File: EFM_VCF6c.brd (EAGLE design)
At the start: 100 x 80.6 mm, 69 parts, among them IC1 LM13700N, Q1 2N3904, Q2 2N3904, Q3 2N3904, Q4 2N3904, Q5 2N3906, U1 POWER

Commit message: fix and mod for self res
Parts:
- Q3: value 2N3904 -> 2N3906; device transistor-npn:TO92 -> transistor-pnp:TO92
- R26: value 47k -> 100k
- moved Q4 31.3 mm to (57.8, 46.4), turned to 0 degrees
- moved Q2 25.3 mm to (27.9, 55.9), turned to 90 degrees
- moved Q3 5.75 mm to (52.1, 47.0), turned to 180 degrees
- moved C6 0.25 mm to (63.5, 61.2)
- moved C7 0.25 mm to (55.9, 61.2)
- moved C8 0.25 mm to (48.3, 61.2)
- moved C9 0.25 mm to (40.6, 61.2)
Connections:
- net -12V: now also Q3.1; no longer Q2.1
- net GND: now also Q4.3; no longer Q3.3
- net N$16: now also Q3.2; no longer Q2.2
- net N$20: now also Q2.1; no longer Q4.1
- net N$26: now also Q2.2; no longer Q4.2
- net N$3: now also Q4.1; no longer Q3.1
- net N$4: now also Q2.3; no longer Q4.3
- net N$8: now also Q3.3, Q4.2; no longer Q2.3, Q3.2
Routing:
- net N$8: track 13.7 -> 15.0 mm
- net N$16: track 91.7 -> 90.4 mm
- net -12V: track 98.6 -> 99.7 mm
- net GND: track 389.0 -> 388.4 mm
- net N$11: track 19.5 -> 18.9 mm

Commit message: fixed cv range setting r16
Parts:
- R16: value 10k -> 560k
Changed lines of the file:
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@@
 <element name="R12" library="rcl" package="0207/7" value="1k" x="19.05" y="10.795" rot="R180"/>
 <element name="R17" library="rcl" package="0207/7" value="1k" x="61.595" y="50.165" rot="R270"/>
-<element name="R16" library="rcl" package="0207/7" value="10k" x="70.485" y="46.99" rot="R180"/>
+<element name="R16" library="rcl" package="0207/7" value="560k" x="70.485" y="46.99" rot="R180"/>
 <element name="R10" library="rcl" package="0207/7" value="100k" x="26.67" y="11.43" rot="R270"/>
 <element name="R15" library="rcl" package="0207/7" value="1k" x="21.59" y="21.59"/>

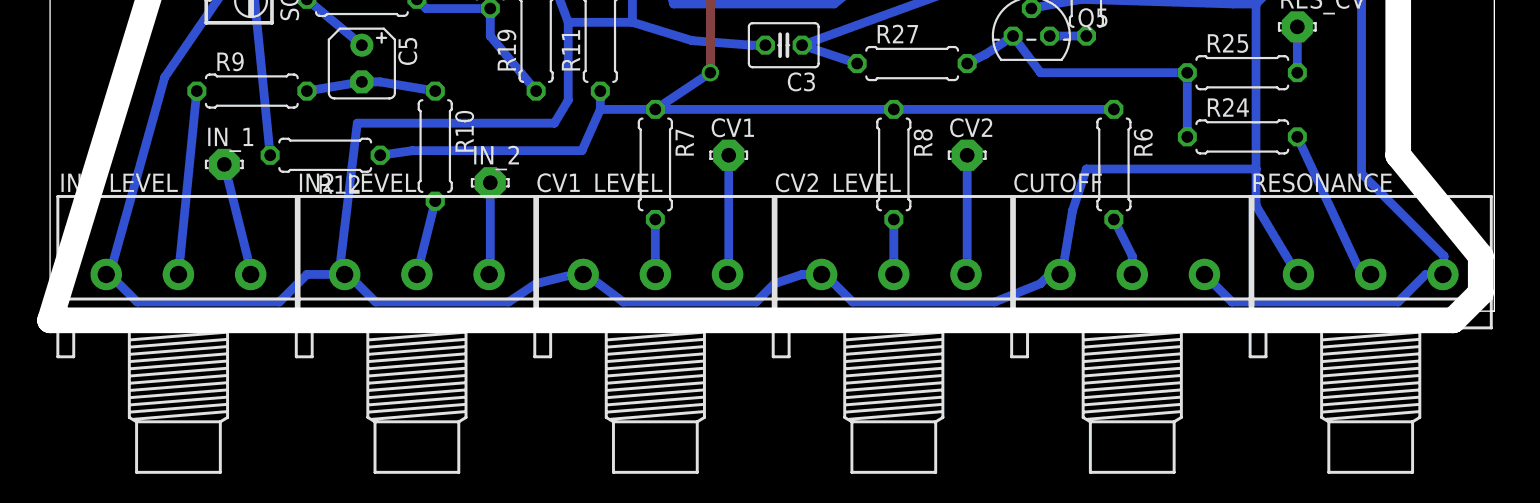
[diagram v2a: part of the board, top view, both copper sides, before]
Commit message: spread out pots and added panel
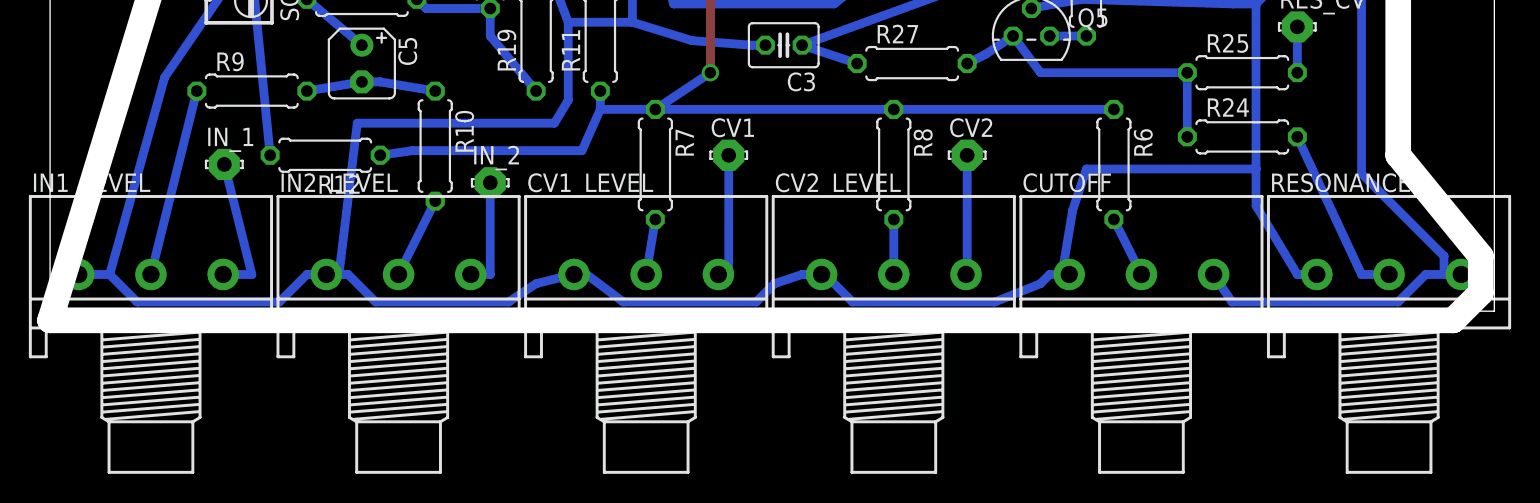
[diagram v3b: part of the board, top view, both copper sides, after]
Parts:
- moved IN1_LEVEL 1.91 mm to (6.99, 2.54)
- moved IN2_LEVEL 1.27 mm to (24.1, 2.54)
- moved RESONANCE 1.27 mm to (92.7, 2.54)
- moved CV1_LEVEL 0.63 mm to (41.3, 2.54)
- moved CUTOFF 0.63 mm to (75.6, 2.54)
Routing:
- net GND: track 388.4 -> 393.2 mm
- net N$58: track 7.93 -> 9.84 mm
- net N$34: track 6.43 -> 7.70 mm
- net N$23: track 11.1 -> 12.4 mm
- net N$38: track 241.8 -> 242.7 mm
- net N$59: track 8.34 -> 8.97 mm
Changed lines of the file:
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@@
 <element name="C8" library="rcl" package="C025-030X050" value="0.1uF" x="48.26" y="61.214"/>
 <element name="C7" library="rcl" package="C025-030X050" value="0.1uF" x="55.88" y="61.214"/>
-<element name="CUTOFF" library="pot" package="3RP/1610N" value="100k" x="74.93" y="2.54"/>
+<element name="CUTOFF" library="pot" package="3RP/1610N" value="100k" x="75.565" y="2.54"/>
 <element name="CV1" library="solpad" package="LSP10" value="LSP10" x="46.99" y="10.795"/>
-<element name="CV1_LEVEL" library="pot" package="3RP/1610N" value="100k" x="41.91" y="2.54"/>
+<element name="CV1_LEVEL" library="pot" package="3RP/1610N" value="100k" x="41.275" y="2.54"/>
 <element name="CV1_NORM" library="solpad" package="LSP10" value="LSP10" x="74.93" y="34.29"/>
 <element name="CV2" library="solpad" package="LSP10" value="LSP10" x="63.5" y="10.795"/>
@@
 <element name="IC1" library="synthdiy updated imperial" package="DIL16" value="LM13700N" x="57.15" y="33.02" rot="R180"/>
 <element name="IN_1" library="solpad" package="LSP10" value="LSP10" x="12.065" y="10.16"/>
-<element name="IN1_LEVEL" library="pot" package="3RP/1610N" value="100k" x="8.89" y="2.54"/>
+<element name="IN1_LEVEL" library="pot" package="3RP/1610N" value="100k" x="6.985" y="2.54"/>
 <element name="IN_2" library="solpad" package="LSP10" value="LSP10" x="30.48" y="8.89"/>
-<element name="IN2_LEVEL" library="pot" package="3RP/1610N" value="100k" x="25.4" y="2.54"/>
+<element name="IN2_LEVEL" library="pot" package="3RP/1610N" value="100k" x="24.13" y="2.54"/>
 <element name="OUT" library="solpad" package="LSP10" value="LSP10" x="40.64" y="46.99"/>
 <element name="Q1" library="transistor-npn" package="TO92" value="2N3904" x="28.575" y="61.595" rot="R90"/>
@@
 <element name="R9" library="rcl" package="0207/7" value="100k" x="13.97" y="15.24"/>
 <element name="R6" library="rcl" package="0207/7" value="100k" x="73.66" y="10.16" rot="R270"/>
-<element name="RESONANCE" library="pot" package="3RP/1610N" value="100k" x="91.44" y="2.54"/>
+<element name="RESONANCE" library="pot" package="3RP/1610N" value="100k" x="92.71" y="2.54"/>
 <element name="RES_CV" library="solpad" package="LSP10" value="LSP10" x="86.36" y="19.685"/>
 <element name="SCALE_TRIM" library="rcl" package="RTRIM64W" value="2k" x="13.335" y="24.765" rot="R180"/>
@@
 <wire x1="83.5025" y1="9.8425" x2="83.5025" y2="21.2725" width="0.6096" layer="16"/>
 <wire x1="86.36" y1="2.54" x2="83.5025" y2="7.3025" width="0.6096" layer="16"/>
-<wire x1="86.36" y1="2.54" x2="86.44" y2="2.54" width="0.6096" layer="16"/>
+<wire x1="86.36" y1="2.54" x2="87.71" y2="2.54" width="0.6096" layer="16"/>
 <wire x1="70.1675" y1="3.175" x2="70.1675" y2="2.54" width="0.6096" layer="16"/>
 <wire x1="70.8025" y1="6.985" x2="70.1675" y2="3.175" width="0.6096" layer="16"/>
 <wire x1="71.755" y1="9.8425" x2="70.8025" y2="6.985" width="0.6096" layer="16"/>
 <wire x1="83.5025" y1="9.8425" x2="71.755" y2="9.8425" width="0.6096" layer="16"/>
-<wire x1="70.1675" y1="2.54" x2="69.93" y2="2.54" width="0.6096" layer="16"/>
+<wire x1="70.1675" y1="2.54" x2="70.565" y2="2.54" width="0.6096" layer="16"/>
 <wire x1="88.9" y1="36.83" x2="86.36" y2="38.1" width="0.6096" layer="16"/>
 <wire x1="88.9" y1="26.67" x2="88.9" y2="36.83" width="0.6096" layer="16"/>
@@
 <wire x1="7.9375" y1="16.1925" x2="12.065" y2="22.225" width="0.6096" layer="16"/>
 <wire x1="4.1275" y1="2.54" x2="7.9375" y2="16.1925" width="0.6096" layer="16"/>
-<wire x1="17.78" y1="2.54" x2="20.0025" y2="2.54" width="0.6096" layer="16"/>
-<wire x1="20.0025" y1="2.54" x2="20.4" y2="2.54" width="0.6096" layer="16"/>
+<wire x1="17.78" y1="2.54" x2="19.13" y2="2.54" width="0.6096" layer="16"/>
+<wire x1="20.0025" y1="2.54" x2="19.13" y2="2.54" width="0.6096" layer="16"/>
 <wire x1="15.875" y1="0.635" x2="17.78" y2="2.54" width="0.6096" layer="16"/>
 <wire x1="6.0325" y1="0.635" x2="15.875" y2="0.635" width="0.6096" layer="16"/>
 <wire x1="4.1275" y1="2.54" x2="6.0325" y2="0.635" width="0.6096" layer="16"/>
-<wire x1="4.1275" y1="2.54" x2="3.89" y2="2.54" width="0.6096" layer="16"/>
-<wire x1="36.195" y1="2.54" x2="36.91" y2="2.54" width="0.6096" layer="16"/>
+<wire x1="4.1275" y1="2.54" x2="1.985" y2="2.54" width="0.6096" layer="16"/>
+<wire x1="36.195" y1="2.54" x2="36.275" y2="2.54" width="0.6096" layer="16"/>
 <wire x1="33.655" y1="1.905" x2="36.195" y2="2.54" width="0.6096" layer="16"/>
 <wire x1="31.75" y1="0.635" x2="33.655" y2="1.905" width="0.6096" layer="16"/>
 <wire x1="22.5425" y1="0.635" x2="31.75" y2="0.635" width="0.6096" layer="16"/>
 <wire x1="20.6375" y1="2.54" x2="22.5425" y2="0.635" width="0.6096" layer="16"/>
-<wire x1="20.6375" y1="2.54" x2="20.4" y2="2.54" width="0.6096" layer="16"/>
+<wire x1="20.6375" y1="2.54" x2="19.13" y2="2.54" width="0.6096" layer="16"/>
 <wire x1="52.07" y1="2.54" x2="53.42" y2="2.54" width="0.6096" layer="16"/>
 <wire x1="50.165" y1="1.905" x2="52.07" y2="2.54" width="0.6096" layer="16"/>
@@
 <wire x1="39.6875" y1="0.635" x2="48.895" y2="0.635" width="0.6096" layer="16"/>
 <wire x1="37.1475" y1="2.54" x2="39.6875" y2="0.635" width="0.6096" layer="16"/>
-<wire x1="37.1475" y1="2.54" x2="36.91" y2="2.54" width="0.6096" layer="16"/>
+<wire x1="37.1475" y1="2.54" x2="36.275" y2="2.54" width="0.6096" layer="16"/>
 <wire x1="35.8775" y1="14.605" x2="35.8775" y2="20.0025" width="0.6096" layer="16"/>
 <wire x1="34.925" y1="13.0175" x2="35.8775" y2="14.605" width="0.6096" layer="16"/>
 <wire x1="21.2725" y1="13.0175" x2="34.925" y2="13.0175" width="0.6096" layer="16"/>
 <wire x1="20.0025" y1="2.54" x2="21.2725" y2="13.0175" width="0.6096" layer="16"/>
-<wire x1="69.215" y1="2.54" x2="69.93" y2="2.54" width="0.6096" layer="16"/>
+<wire x1="69.215" y1="2.54" x2="70.565" y2="2.54" width="0.6096" layer="16"/>
 <wire x1="68.58" y1="1.905" x2="69.215" y2="2.54" width="0.6096" layer="16"/>
 <wire x1="65.405" y1="0.635" x2="68.58" y2="1.905" width="0.6096" layer="16"/>
@@
 <contactref element="IN2_LEVEL" pad="2"/>
 <contactref element="R10" pad="2"/>
-<wire x1="25.4" y1="2.54" x2="26.67" y2="7.62" width="0.6096" layer="16"/>
+<wire x1="24.13" y1="2.54" x2="26.67" y2="7.62" width="0.6096" layer="16"/>
 </signal>
 <signal name="N$6">
@@
 <contactref element="IN_2" pad="MP"/>
 <wire x1="30.48" y1="2.54" x2="30.48" y2="8.89" width="0.6096" layer="16"/>
-<wire x1="30.48" y1="2.54" x2="30.4" y2="2.54" width="0.6096" layer="16"/>
+<wire x1="30.48" y1="2.54" x2="29.13" y2="2.54" width="0.6096" layer="16"/>
 </signal>
 <signal name="N$54">
@@
 <contactref element="CUTOFF" pad="2"/>
 <contactref element="R6" pad="2"/>
-<wire x1="74.93" y1="3.81" x2="73.66" y2="6.35" width="0.6096" layer="16"/>
-<wire x1="74.93" y1="2.54" x2="74.93" y2="3.81" width="0.6096" layer="16"/>
+<wire x1="75.565" y1="2.54" x2="73.66" y2="6.35" width="0.6096" layer="16"/>
 </signal>
 <signal name="N$57">
 <contactref element="IN1_LEVEL" pad="2"/>
 <contactref element="R9" pad="1"/>
-<wire x1="8.89" y1="2.54" x2="10.16" y2="15.24" width="0.6096" layer="16"/>
+<wire x1="6.985" y1="2.54" x2="10.16" y2="15.24" width="0.6096" layer="16"/>
 </signal>
 <signal name="N$58">
@@
 <contactref element="IN_1" pad="MP"/>
 <wire x1="13.97" y1="2.54" x2="12.065" y2="10.16" width="0.6096" layer="16"/>
-<wire x1="13.97" y1="2.54" x2="13.89" y2="2.54" width="0.6096" layer="16"/>
+<wire x1="13.97" y1="2.54" x2="11.985" y2="2.54" width="0.6096" layer="16"/>
 </signal>
 <signal name="N$53">
 <contactref element="R7" pad="2"/>
 <contactref element="CV1_LEVEL" pad="2"/>
-<wire x1="41.91" y1="2.54" x2="41.91" y2="6.35" width="0.6096" layer="16"/>
+<wire x1="41.275" y1="2.54" x2="41.91" y2="6.35" width="0.6096" layer="16"/>
 </signal>
 <signal name="N$59">
@@
 <contactref element="CV1_LEVEL" pad="3"/>
 <wire x1="46.99" y1="2.54" x2="46.99" y2="10.795" width="0.6096" layer="16"/>
-<wire x1="46.99" y1="2.54" x2="46.91" y2="2.54" width="0.6096" layer="16"/>
+<wire x1="46.99" y1="2.54" x2="46.275" y2="2.54" width="0.6096" layer="16"/>
 </signal>
 <signal name="N$1">
@@
 <contactref element="R24" pad="2"/>
 <wire x1="90.805" y1="2.54" x2="86.36" y2="12.065" width="0.6096" layer="16"/>
-<wire x1="91.44" y1="2.54" x2="90.805" y2="2.54" width="0.6096" layer="16"/>
+<wire x1="92.71" y1="2.54" x2="90.805" y2="2.54" width="0.6096" layer="16"/>
 </signal>
 <signal name="N$24">
@@
 <wire x1="76.2" y1="51.435" x2="76.2" y2="57.15" width="0.6096" layer="16"/>
 <wire x1="76.2" y1="57.15" x2="77.47" y2="58.42" width="0.6096" layer="16"/>
-<wire x1="96.44" y1="2.54" x2="95.25" y2="2.54" width="0.6096" layer="16"/>
+<wire x1="97.71" y1="2.54" x2="95.25" y2="2.54" width="0.6096" layer="16"/>
 <wire x1="95.25" y1="2.54" x2="93.345" y2="0.635" width="0.6096" layer="16"/>
 <wire x1="93.345" y1="0.635" x2="81.835" y2="0.635" width="0.6096" layer="16"/>
-<wire x1="81.835" y1="0.635" x2="79.93" y2="2.54" width="0.6096" layer="16"/>
+<wire x1="81.835" y1="0.635" x2="80.565" y2="2.54" width="0.6096" layer="16"/>
 <wire x1="78.74" y1="48.26" x2="74.295" y2="46.99" width="0.6096" layer="16"/>
 <wire x1="31.115" y1="43.815" x2="31.75" y2="49.53" width="0.6096" layer="16"/>
 <wire x1="35.56" y1="52.07" x2="32.385" y2="50.165" width="0.6096" layer="16"/>
 <wire x1="32.385" y1="50.165" x2="31.75" y2="49.53" width="0.6096" layer="16"/>
-<wire x1="96.52" y1="2.54" x2="96.44" y2="2.54" width="0" layer="19" extent="16-16"/>
+<wire x1="96.52" y1="2.54" x2="97.71" y2="2.54" width="0" layer="19" extent="16-16"/>
 </signal>
 </signals>
